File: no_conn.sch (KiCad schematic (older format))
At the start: 0 parts

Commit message: WIP: point before we change to OSH/relaxed process
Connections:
- no-connect marks 146 -> 56

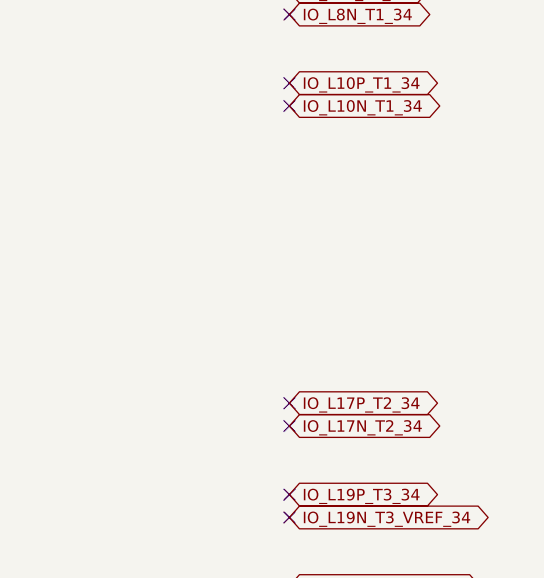
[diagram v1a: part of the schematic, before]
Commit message: re-routed with more relaxed specs (that eurocircuits can also meet)
No chance with OSH, however...

Going to place stuff on the board now...
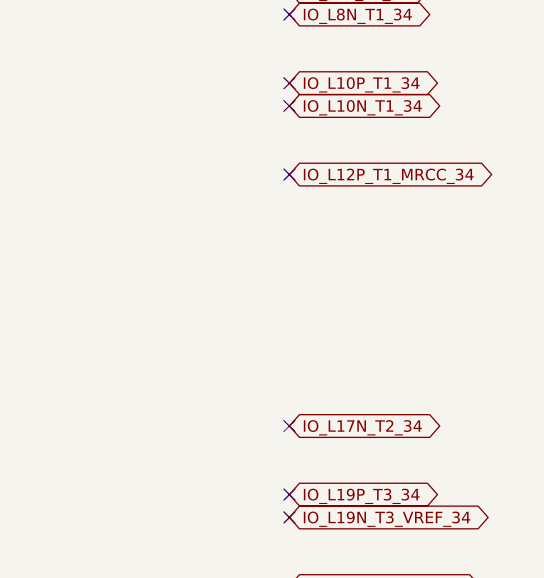
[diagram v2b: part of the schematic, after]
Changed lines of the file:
@@
 Text GLabel 9750 4450 2    50   BiDi ~ 0
 IO_L17N_T2_34
-Text GLabel 9750 4350 2    50   BiDi ~ 0
-IO_L17P_T2_34
 Text GLabel 9750 5250 2    50   BiDi ~ 0
 IO_L21N_T3_DQS_34
@@
 NoConn ~ 9750 2950
 NoConn ~ 9750 3050
-NoConn ~ 9750 4350
+NoConn ~ 9750 3350
 NoConn ~ 9750 4450
 NoConn ~ 9750 4750
@@
 Text GLabel 9750 1850 2    50   BiDi ~ 0
 IO_L4N_T0_34
+Text GLabel 9750 3350 2    50   BiDi ~ 0
+IO_L12P_T1_MRCC_34
 $EndSCHEMATC

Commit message: further work...
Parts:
- added TP1, TP10, TP11, TP12, TP13, TP2, TP3, TP4, TP5, TP6, TP7, TP8: Dummy End, proj_footprints:endpoint_0.1mm, symbol Connector:TestPoint_Small
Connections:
- net IO_L13P_T2_MRCC_14: now also TP4.1
- net IO_L17N_T2_34: now also TP10.1
- net IO_L17P_T2_A14_D30_14: now also TP5.1
- net IO_L19N_T3_A09_D25_VREF_14: now also TP6.1
- net IO_L19P_T3_34: now also TP11.1
- net IO_L20N_T3_A07_D23_14: now also TP8.1
- net IO_L20P_T3_A08_D24_14: now also TP7.1
- net IO_L21N_T3_DQS_34: now also TP12.1
- net IO_L9P_T1_DQS_AD3P_15: now also TP3.1
- new net IO_L22P_T3_34: TP13.1
- new net IO_L7N_T1_AD2N_15: TP2.1
- new net IO_L7P_T1_AD2P_15: TP1.1
- no-connect marks 56 -> 42
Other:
- note added: "AUX\nADC"
- note added: "Testpoints on this page are\npins that are currently unused\nbut have been routed to the\nedge of the FPGA."
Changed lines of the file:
@@
 $Descr A4 11693 8268
 encoding utf-8
-Sheet 10 18
+Sheet 10 20
 Title ""
 Date ""
@@
 Text GLabel 9750 1050 2    50   BiDi ~ 0
 IO_0_34
-Text GLabel 9750 1750 2    50   BiDi ~ 0
-IO_L4P_T0_34
 Text GLabel 9750 1250 2    50   BiDi ~ 0
 IO_L1N_T0_34
 Text GLabel 9750 1150 2    50   BiDi ~ 0
 IO_L1P_T0_34
-Text GLabel 9750 2050 2    50   BiDi ~ 0
-IO_L5N_T0_34
 Text GLabel 9750 1950 2    50   BiDi ~ 0
 IO_L5P_T0_34
 Text GLabel 9750 2150 2    50   BiDi ~ 0
 IO_L6P_T0_34
-Text GLabel 9750 2950 2    50   BiDi ~ 0
-IO_L10P_T1_34
 Text GLabel 9750 2250 2    50   BiDi ~ 0
 IO_L6N_T0_VREF_34
@@
 NoConn ~ 9750 1350
 NoConn ~ 9750 1450
-NoConn ~ 9750 1750
-NoConn ~ 9750 1850
+NoConn ~ 9750 5850
 NoConn ~ 9750 1950
-NoConn ~ 9750 2050
+NoConn ~ 9750 5450
 NoConn ~ 9750 2150
 NoConn ~ 9750 2250
 NoConn ~ 9750 2550
 NoConn ~ 9750 2650
-NoConn ~ 9750 2950
+NoConn ~ 9750 5750
 NoConn ~ 9750 3050
-NoConn ~ 9750 3350
-NoConn ~ 9750 4450
-NoConn ~ 9750 4750
 NoConn ~ 9750 4850
 NoConn ~ 9750 5150
-NoConn ~ 9750 5250
 NoConn ~ 9750 5550
-Text GLabel 2300 1700 0    50   BiDi ~ 0
-IO_L3N_T0_DQS_AD1N_15
 Text GLabel 2300 3000 0    50   BiDi ~ 0
 IO_L10P_T1_AD11P_15
@@
 Text GLabel 2300 1300 0    50   BiDi ~ 0
 IO_L1N_T0_AD0N_15
-Text GLabel 2300 1500 0    50   BiDi ~ 0
-IO_L2N_T0_AD8N_15
 Text GLabel 2300 1100 0    50   BiDi ~ 0
 IO_0_15
@@
 NoConn ~ 2300 1300
 NoConn ~ 2300 1400
-NoConn ~ 2300 1500
 NoConn ~ 2300 1600
-NoConn ~ 2300 1700
 NoConn ~ 2300 1800
 NoConn ~ 2300 2200
 NoConn ~ 2300 2300
-NoConn ~ 2300 2800
 NoConn ~ 2300 3000
 NoConn ~ 2300 3300
 NoConn ~ 2300 3500
 NoConn ~ 2300 5000
-NoConn ~ 2300 5100
 NoConn ~ 2300 5200
 NoConn ~ 2300 5300
@@
 Text GLabel 3250 3600 2    50   BiDi ~ 0
 IO_L13P_T2_MRCC_14
-Text GLabel 3250 5000 2    50   BiDi ~ 0
-IO_L20P_T3_A08_D24_14
 Text GLabel 3250 4400 2    50   BiDi ~ 0
 IO_L17P_T2_A14_D30_14
@@
 NoConn ~ 3250 2100
 NoConn ~ 3250 3400
-NoConn ~ 3250 3600
-NoConn ~ 3250 4400
 NoConn ~ 3250 4800
-NoConn ~ 3250 4900
-NoConn ~ 3250 5000
-NoConn ~ 3250 5100
 NoConn ~ 3250 5800
 NoConn ~ 3250 5900
-Text GLabel 9750 1850 2    50   BiDi ~ 0
-IO_L4N_T0_34
-Text GLabel 9750 3350 2    50   BiDi ~ 0
-IO_L12P_T1_MRCC_34
+Text GLabel 2300 2500 0    50   BiDi ~ 0
+IO_L7N_T1_AD2N_15
+Text GLabel 9750 5350 2    50   BiDi ~ 0
+IO_L22P_T3_34
+Text GLabel 9750 5850 2    50   BiDi ~ 0
+IO_L24N_T3_34
+Text GLabel 9750 5450 2    50   BiDi ~ 0
+IO_L22N_T3_34
+Text GLabel 9750 5750 2    50   BiDi ~ 0
+IO_L24P_T3_34
+$Comp
+L Connector:TestPoint_Small TP1
+U 1 1 6289A23F
+P 2450 2400
+F 0 "TP1" H 2498 2400 50  0000 L CNN
+F 1 "Dummy End" H 2498 2355 50  0001 L CNN
+F 2 "proj_footprints:endpoint_0.1mm" H 2650 2400 50  0001 C CNN
+F 3 "~" H 2650 2400 50  0001 C CNN
+	1    2450 2400
+	1    0    0    -1
+$EndComp
+Wire Wire Line
+	2300 2400 2450 2400
+$Comp
+L Connector:TestPoint_Small TP2
+U 1 1 6289DCF7
+P 2450 2500
+F 0 "TP2" H 2498 2500 50  0000 L CNN
+F 1 "Dummy End" H 2498 2455 50  0001 L CNN
+F 2 "proj_footprints:endpoint_0.1mm" H 2650 2500 50  0001 C CNN
+F 3 "~" H 2650 2500 50  0001 C CNN
+	1    2450 2500
+	1    0    0    -1
+$EndComp
+$Comp
+L Connector:TestPoint_Small TP3
+U 1 1 6289FB49
+P 2450 2800
+F 0 "TP3" H 2498 2800 50  0000 L CNN
+F 1 "Dummy End" H 2498 2755 50  0001 L CNN
+F 2 "proj_footprints:endpoint_0.1mm" H 2650 2800 50  0001 C CNN
+F 3 "~" H 2650 2800 50  0001 C CNN
+	1    2450 2800
+	1    0    0    -1
+$EndComp
+$Comp
+L Connector:TestPoint_Small TP4
+U 1 1 6289FE0A
+P 3100 3600
+F 0 "TP4" V 3100 3750 50  0000 C CNN
+F 1 "Dummy End" H 3148 3555 50  0001 L CNN
+F 2 "proj_footprints:endpoint_0.1mm" H 3300 3600 50  0001 C CNN
+F 3 "~" H 3300 3600 50  0001 C CNN
+	1    3100 3600
+	0    -1   1    0
+$EndComp
+Wire Wire Line
+	3250 3600 3100 3600
+Wire Wire Line
+	2300 2800 2450 2800
+Wire Wire Line
+	2300 2500 2450 2500
+$Comp
+L Connector:TestPoint_Small TP6
+U 1 1 628A12AD
+P 3100 4900
+F 0 "TP6" V 3100 5100 50  0000 C CNN
+F 1 "Dummy End" H 3148 4855 50  0001 L CNN
+F 2 "proj_footprints:endpoint_0.1mm" H 3300 4900 50  0001 C CNN
+F 3 "~" H 3300 4900 50  0001 C CNN
+	1    3100 4900
+	0    -1   1    0
+$EndComp
+$Comp
+L Connector:TestPoint_Small TP5
+U 1 1 628A1759
+P 3100 4400
+F 0 "TP5" V 3100 4600 50  0000 C CNN
+F 1 "Dummy End" H 3148 4355 50  0001 L CNN
+F 2 "proj_footprints:endpoint_0.1mm" H 3300 4400 50  0001 C CNN
+F 3 "~" H 3300 4400 50  0001 C CNN
+	1    3100 4400
+	0    -1   1    0
+$EndComp
+$Comp
+L Connector:TestPoint_Small TP8
+U 1 1 628A1A9D
+P 3100 5100
+F 0 "TP8" V 3100 5300 50  0000 C CNN
+F 1 "Dummy End" H 3148 5055 50  0001 L CNN
+F 2 "proj_footprints:endpoint_0.1mm" H 3300 5100 50  0001 C CNN
+F 3 "~" H 3300 5100 50  0001 C CNN
+	1    3100 5100
+	0    -1   1    0
+$EndComp
+Text GLabel 3250 5000 2    50   BiDi ~ 0
+IO_L20P_T3_A08_D24_14
+$Comp
+L Connector:TestPoint_Small TP7
+U 1 1 628A21CE
+P 3100 5000
+F 0 "TP7" V 3100 5200 50  0000 C CNN
+F 1 "Dummy End" H 3148 4955 50  0001 L CNN
+F 2 "proj_footprints:endpoint_0.1mm" H 3300 5000 50  0001 C CNN
+F 3 "~" H 3300 5000 50  0001 C CNN
+	1    3100 5000
+	0    -1   1    0
+$EndComp
+$Comp
+L Connector:TestPoint_Small TP13
+U 1 1 628A33C3
+P 9600 5350
+F 0 "TP13" V 9600 5550 50  0000 C CNN
+F 1 "Dummy End" H 9648 5305 50  0001 L CNN
+F 2 "proj_footprints:endpoint_0.1mm" H 9800 5350 50  0001 C CNN
+F 3 "~" H 9800 5350 50  0001 C CNN
+	1    9600 5350
+	0    -1   1    0
+$EndComp
+$Comp
+L Connector:TestPoint_Small TP12
+U 1 1 628A3D53
+P 9600 5250
+F 0 "TP12" V 9600 5450 50  0000 C CNN
+F 1 "Dummy End" H 9648 5205 50  0001 L CNN
+F 2 "proj_footprints:endpoint_0.1mm" H 9800 5250 50  0001 C CNN
+F 3 "~" H 9800 5250 50  0001 C CNN
+	1    9600 5250
+	0    -1   1    0
+$EndComp
+$Comp
+L Connector:TestPoint_Small TP11
+U 1 1 628A3F5A
+P 9600 4750
+F 0 "TP11" V 9600 4950 50  0000 C CNN
+F 1 "Dummy End" H 9648 4705 50  0001 L CNN
+F 2 "proj_footprints:endpoint_0.1mm" H 9800 4750 50  0001 C CNN
+F 3 "~" H 9800 4750 50  0001 C CNN
+	1    9600 4750
+	0    -1   1    0
+$EndComp
+$Comp
+L Connector:TestPoint_Small TP10
+U 1 1 628A47EA
+P 9600 4450
+F 0 "TP10" V 9600 4650 50  0000 C CNN
+F 1 "Dummy End" H 9648 4405 50  0001 L CNN
+F 2 "proj_footprints:endpoint_0.1mm" H 9800 4450 50  0001 C CNN
+F 3 "~" H 9800 4450 50  0001 C CNN
+	1    9600 4450
+	0    -1   1    0
+$EndComp
+Wire Wire Line
+	9600 4450 9750 4450
+Wire Wire Line
+	9600 4750 9750 4750
+Wire Wire Line
+	9600 5250 9750 5250
+Wire Wire Line
+	9600 5350 9750 5350
+Wire Wire Line
+	3100 4400 3250 4400
+Wire Wire Line
+	3100 4900 3250 4900
+Wire Wire Line
+	3100 5000 3250 5000
+Wire Wire Line
+	3100 5100 3250 5100
+Text Notes 4250 7000 0    50   ~ 0
+Testpoints on this page are\npins that are currently unused\nbut have been routed to the\nedge of the FPGA.
+Text GLabel 2300 2400 0    50   BiDi ~ 0
+IO_L7P_T1_AD2P_15
+Text Notes 2700 2550 0    50   ~ 0
+AUX\nADC
 $EndSCHEMATC

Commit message: added 3rd GPIO
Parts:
- removed TP5, TP8: Dummy End, proj_footprints:endpoint_0.1mm, symbol Connector:TestPoint_Small
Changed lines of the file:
@@
 $Descr A4 11693 8268
 encoding utf-8
-Sheet 10 20
+Sheet 10 21
 Title ""
 Date ""
@@
 Text GLabel 3250 3600 2    50   BiDi ~ 0
 IO_L13P_T2_MRCC_14
-Text GLabel 3250 4400 2    50   BiDi ~ 0
-IO_L17P_T2_A14_D30_14
 Text GLabel 3250 5800 2    50   BiDi ~ 0
 IO_L24P_T3_A01_D17_14
-Text GLabel 3250 5100 2    50   BiDi ~ 0
-IO_L20N_T3_A07_D23_14
 Text GLabel 3250 5900 2    50   BiDi ~ 0
 IO_L24N_T3_A00_D16_14
@@
 	0    -1   1    0
 $EndComp
-$Comp
-L Connector:TestPoint_Small TP5
-U 1 1 628A1759
-P 3100 4400
-F 0 "TP5" V 3100 4600 50  0000 C CNN
-F 1 "Dummy End" H 3148 4355 50  0001 L CNN
-F 2 "proj_footprints:endpoint_0.1mm" H 3300 4400 50  0001 C CNN
-F 3 "~" H 3300 4400 50  0001 C CNN
-	1    3100 4400
-	0    -1   1    0
-$EndComp
-$Comp
-L Connector:TestPoint_Small TP8
-U 1 1 628A1A9D
-P 3100 5100
-F 0 "TP8" V 3100 5300 50  0000 C CNN
-F 1 "Dummy End" H 3148 5055 50  0001 L CNN
-F 2 "proj_footprints:endpoint_0.1mm" H 3300 5100 50  0001 C CNN
-F 3 "~" H 3300 5100 50  0001 C CNN
-	1    3100 5100
-	0    -1   1    0
-$EndComp
 Text GLabel 3250 5000 2    50   BiDi ~ 0
 IO_L20P_T3_A08_D24_14
@@
 	9600 5350 9750 5350
 Wire Wire Line
-	3100 4400 3250 4400
-Wire Wire Line
 	3100 4900 3250 4900
 Wire Wire Line
 	3100 5000 3250 5000
-Wire Wire Line
-	3100 5100 3250 5100
 Text Notes 4250 7000 0    50   ~ 0
 Testpoints on this page are\npins that are currently unused\nbut have been routed to the\nedge of the FPGA.
